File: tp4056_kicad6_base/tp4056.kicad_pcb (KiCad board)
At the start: 2 copper layers, 40 x 32 mm, 34 parts, among them J1 Conn_01x01_Female, J2 Conn_01x01_Female, J3 USB_B_Micro, J4 Conn_01x02_Male, J6 Conn_01x05_Male, Q1 AO3401A, Q2 FS8205A, Q3 AO3401A, U1 TP4056, U2 DW01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

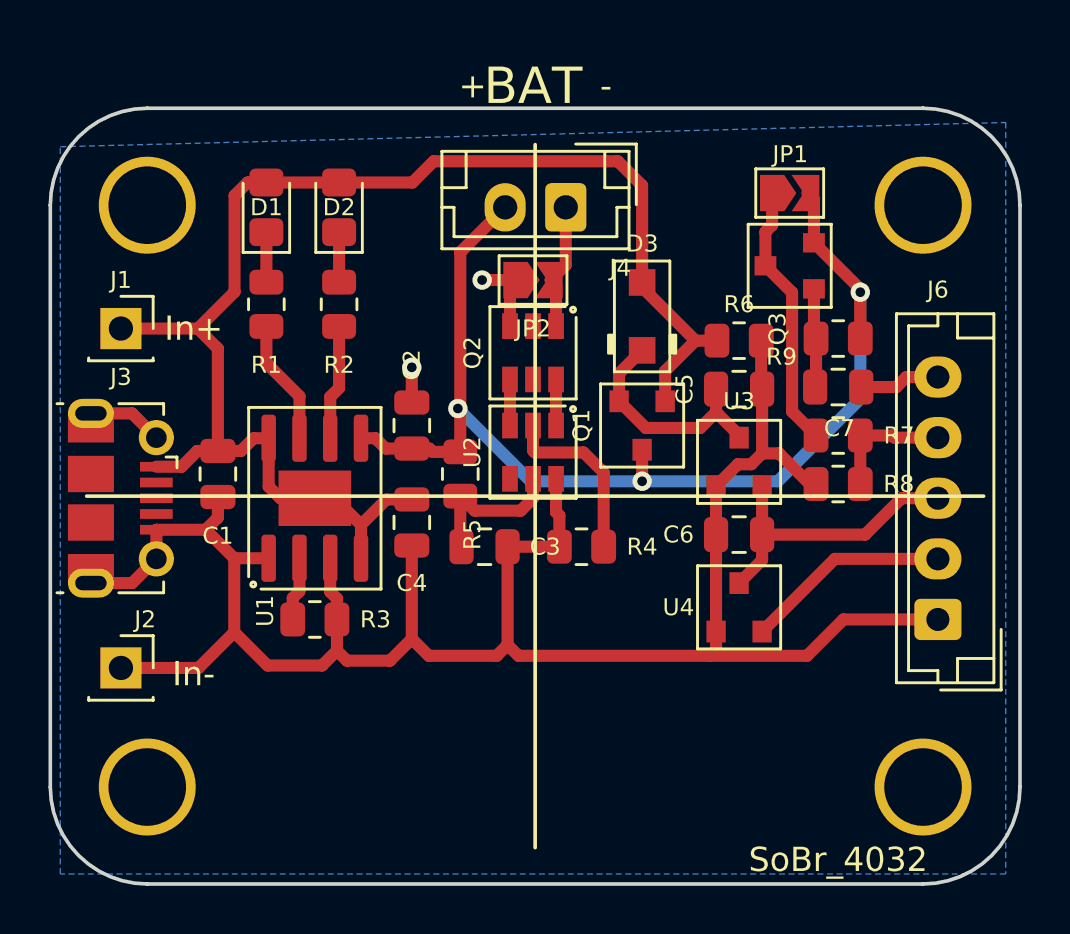
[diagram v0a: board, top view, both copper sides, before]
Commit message: PCB 40x25. To check DRC
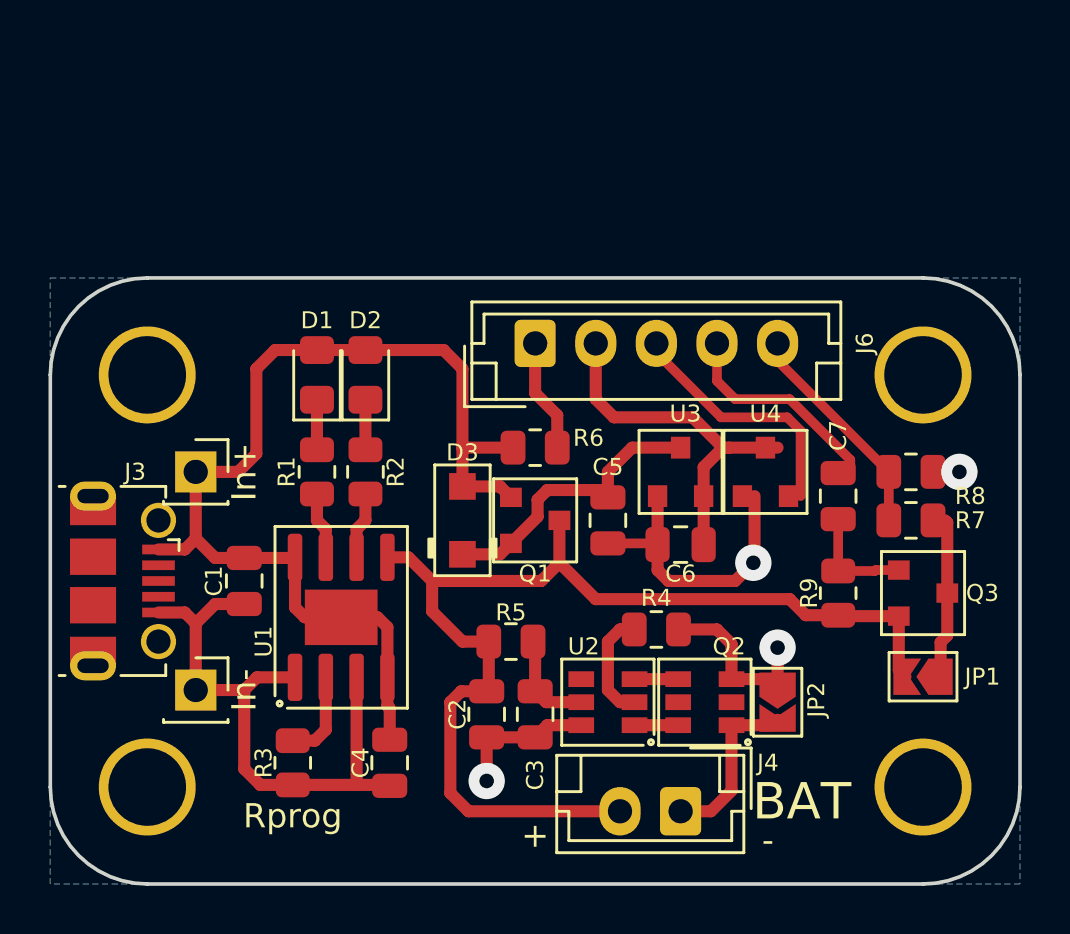
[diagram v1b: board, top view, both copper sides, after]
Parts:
- removed the REF** at (174.0, 113.0)
- added REF**: SoBr_4025, SoBr:SoBr_4025, F.Cu at (194.0, 100.5)
- moved J4 25.4 mm to (200.0, 110.0)
- moved JP1 20.7 mm to (210.0, 104.5), turned to 180 degrees
- moved J6 20.1 mm to (194.0, 90.7), turned to 0 degrees
- moved JP2 20.1 mm to (204.0, 105.5), turned to -90 degrees
- moved Q2 16.1 mm to (201.0, 105.5), turned to 180 degrees
- moved Q3 14.6 mm to (210.0, 101.0), turned to 0 degrees
- moved C2 12.3 mm to (192.0, 106.0), turned to -90 degrees
- moved D3 11.2 mm to (191.0, 98.0)
- moved U2 10.8 mm to (197.0, 105.5), turned to 180 degrees
- moved R9 10.5 mm to (206.5, 101.0), turned to 90 degrees
- moved C4 9.95 mm to (188.0, 108.0)
- moved R6 9.50 mm to (194.0, 95.0)
- moved C5 7.65 mm to (197.0, 98.0), turned to -90 degrees
- moved C3 7.22 mm to (194.0, 106.0), turned to -90 degrees
- moved D1 7.22 mm to (185.0, 92.0)
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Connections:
- J6 pad 2: /RST -> +3.3V
- J6 pad 3: +3.3V -> /RST
- J6 pad 4: /measurment -> /ena_meas
- J6 pad 5: /ena_meas -> /measurment
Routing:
- net Earth: track 92.4 -> 56.6 mm, vias 2 -> 4
- net VBUS: track 59.2 -> 44.4 mm
- net /ena_meas: track 3.33 -> 8.95 mm
- net Net-(JP1-Pad1): track 11.0 -> 6.60 mm
- net /measurment: track 5.24 -> 9.20 mm
- net Net-(R4-Pad2): track 7.38 -> 4.60 mm
- net +3.3V: track 12.3 -> 15.0 mm
- net VDC: track 9.61 -> 12.1 mm
- net Net-(R1-Pad2): track 5.18 -> 2.76 mm
- net Net-(C3-Pad1): track 6.37 -> 4.17 mm
- net Net-(R2-Pad2): track 4.76 -> 2.76 mm
- net -BATT: track 5.25 -> 7.15 mm
- net /RST: track 8.49 -> 10.4 mm
- net Net-(R3-Pad1): track 2.64 -> 3.71 mm
- net +BATT: track 47.0 -> 46.1 mm, vias 3 -> 0
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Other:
- board size 40 x 32 mm -> 40 x 25 mm
- board text added: "Rprog"

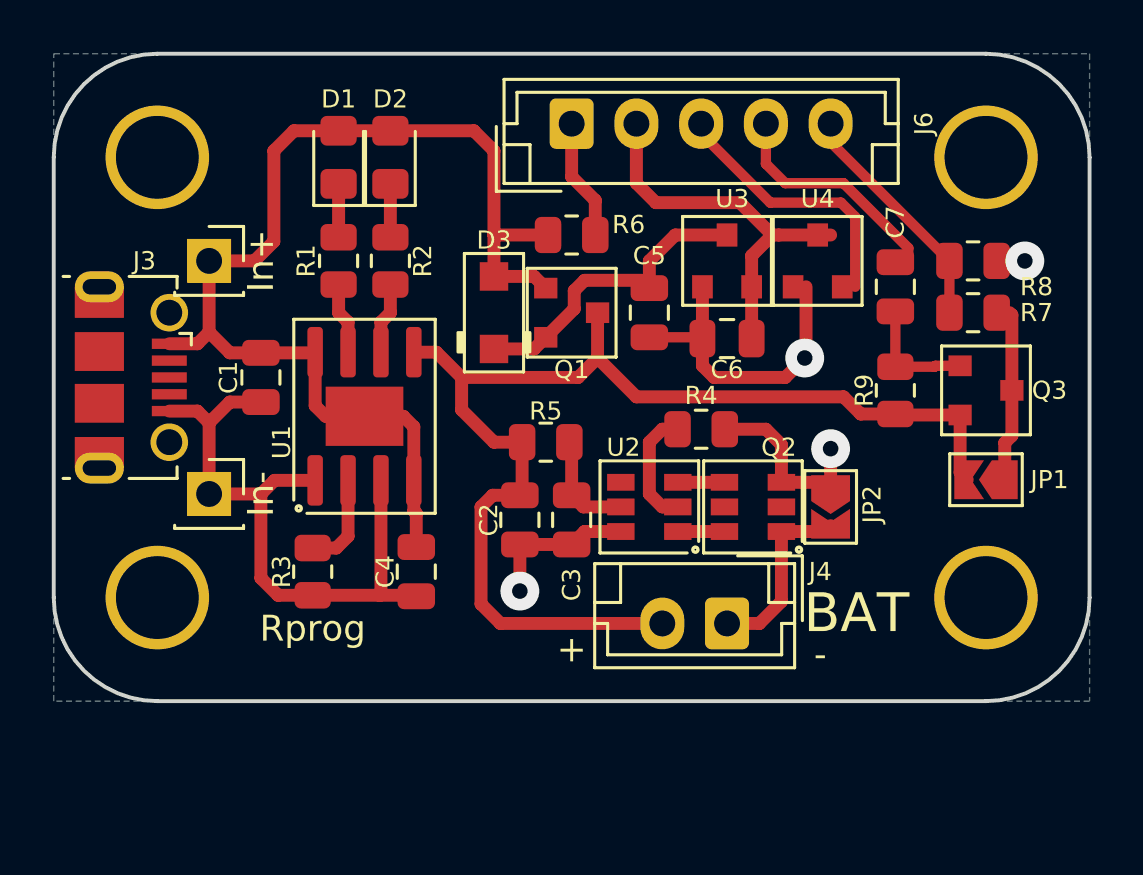
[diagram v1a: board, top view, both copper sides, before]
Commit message: SCH. Add USB and Wall Power Adaptor
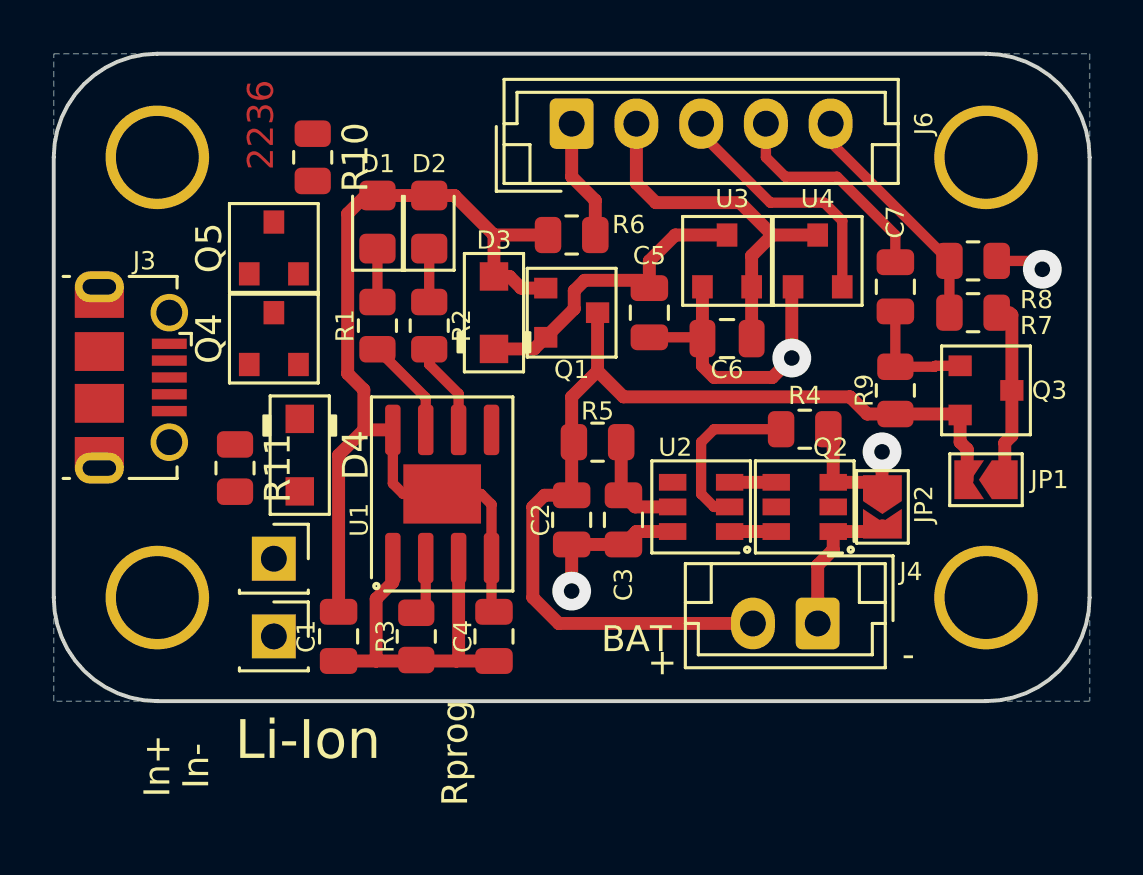
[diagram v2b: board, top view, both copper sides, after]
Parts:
- added D4: MBR1020VL, Diode_SMD_AKL:D_SOD-123F, F.Cu at (183.5, 103.5)
- added Q4: AO3401A, Package_TO_SOT_SMD_AKL:SOT-23, F.Cu at (182.5, 99.0)
- added Q5: AO3400A, Package_TO_SOT_SMD_AKL:SOT-23, F.Cu at (182.5, 95.5)
- added R10: 10k, Resistor_SMD:R_0805_2012Metric, F.Cu at (184.0, 92.0)
- added R11: 1k, Resistor_SMD:R_0805_2012Metric, F.Cu at (181.0, 104.0)
- R3: value 10k -> 2k
- moved J1 11.8 mm to (182.5, 107.5)
- moved C1 10.4 mm to (185.0, 110.5)
- moved J2 6.04 mm to (182.5, 110.5)
- moved R3 4.72 mm to (188.0, 110.5)
- moved U1 4.24 mm to (189.0, 105.0)
- moved R4 4.00 mm to (203.0, 102.5)
- moved C4 3.91 mm to (191.0, 110.5)
- moved J4 3.50 mm to (203.5, 110.0)
- moved D1 2.92 mm to (186.5, 94.5)
- moved D2 2.92 mm to (188.5, 94.5)
- moved R1 2.92 mm to (186.5, 98.5)
- moved R2 2.92 mm to (188.5, 98.5)
- moved C2 2.00 mm to (194.0, 106.0)
- moved C3 2.00 mm to (196.0, 106.0)
- moved JP2 2.00 mm to (206.0, 105.5)
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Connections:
- net Net-(R3-Pad1) renamed /Rprog
- C1 pad 1: VBUS -> VCC
- C4 pad 1: VBUS -> VCC
- D1 pad 2: VBUS -> VCC
- D2 pad 2: VBUS -> VCC
- D3 pad 2: VBUS -> VCC
- J1 pad 1: VBUS -> /Vwall
- J3 pad 1: VBUS -> /Vusb
- Q1 pad 1: VBUS -> VCC
- R6 pad 1: VBUS -> VCC
- U1 pad 4: VBUS -> VCC
- U1 pad 8: VBUS -> VCC
- U1 pad 9: VBUS -> VCC
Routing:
- net VBUS: track 44.4 -> 0.00 mm
- net VCC: track 0.00 -> 40.0 mm
- net Earth: track 56.6 -> 44.2 mm
- net +BATT: track 46.1 -> 39.0 mm
- net Net-(R4-Pad2): track 4.60 -> 6.60 mm
- net /Rprog: track 3.71 -> 2.26 mm
- net -BATT: track 7.15 -> 5.79 mm
- net Net-(R1-Pad2): track 2.76 -> 3.89 mm
- net Net-(R2-Pad2): track 2.76 -> 3.58 mm
- net /RST: track 10.4 -> 9.78 mm
- net +3.3V: track 15.0 -> 14.5 mm
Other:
- board text added: "2236"
- board text added: "Li-Ion"

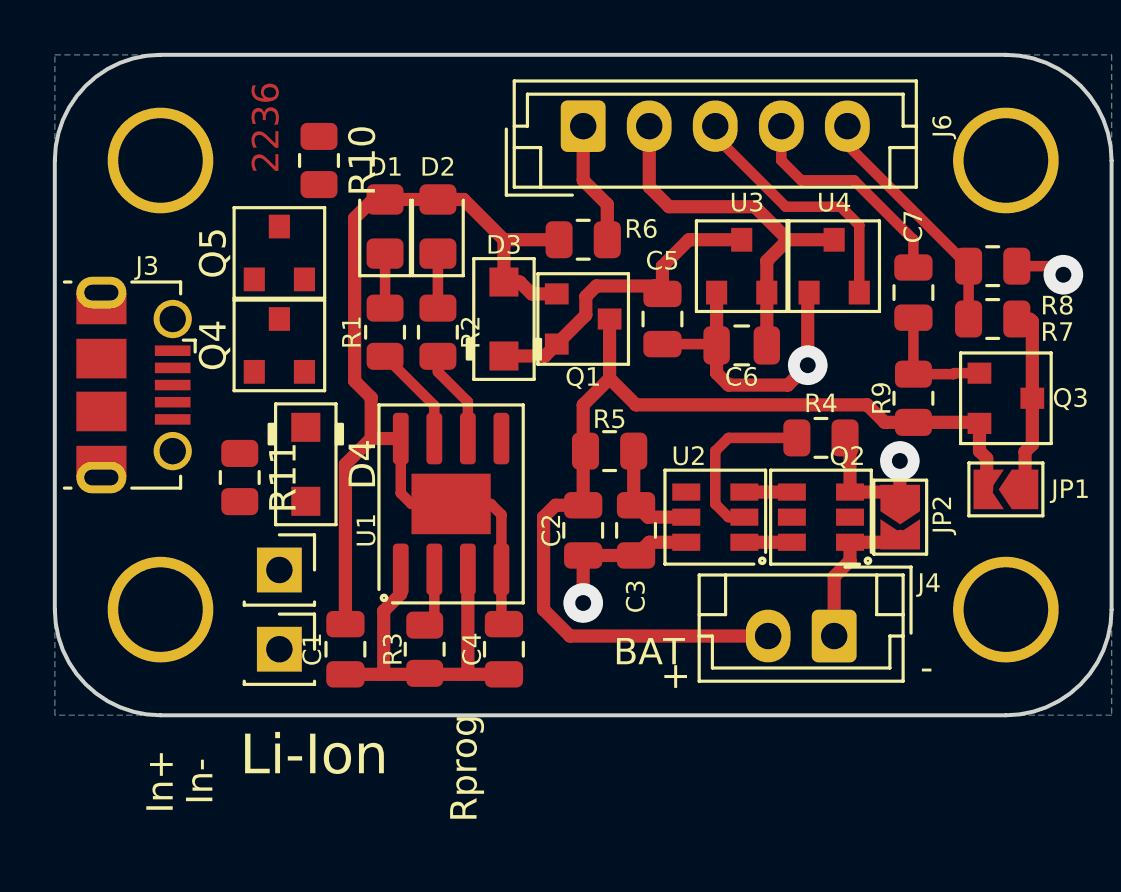
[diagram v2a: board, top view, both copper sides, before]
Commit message: PCB. 40x25. Add wall adpapter option. To final check.
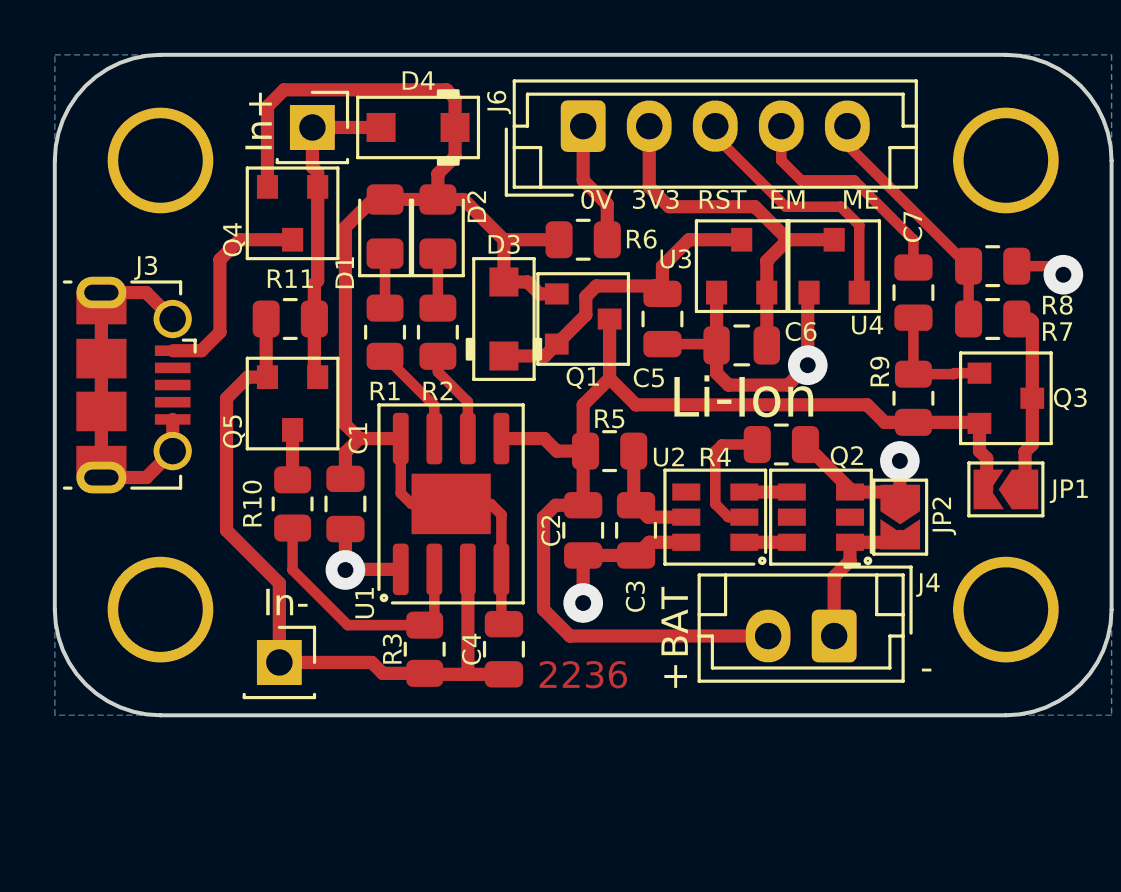
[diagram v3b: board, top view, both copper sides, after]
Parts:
- moved J1 16.8 mm to (183.8, 90.8)
- moved D4 13.4 mm to (187.8, 90.8), turned to 180 degrees
- moved R10 13.0 mm to (183.0, 105.0), turned to 90 degrees
- moved R11 6.30 mm to (182.9, 98.0), turned to 0 degrees
- moved Q5 5.72 mm to (183.0, 101.2), turned to -90 degrees
- moved C1 5.50 mm to (185.0, 105.0)
- moved Q4 5.02 mm to (183.0, 94.0), turned to -90 degrees
- moved R4 1.52 mm to (201.5, 102.8)
- moved J2 0.50 mm to (182.5, 111.0)
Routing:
- net Earth: track 44.2 -> 76.0 mm, vias 4 -> 5
- net /Vwall: track 0.00 -> 12.2 mm
- net VCC: track 40.0 -> 49.5 mm
- net /Vusb: track 0.00 -> 7.89 mm
- net /Rprog: track 2.26 -> 9.72 mm
- net +BATT: track 39.0 -> 42.3 mm
- net Net-(Q5-Pad3): track 0.00 -> 1.89 mm
- net Net-(R4-Pad2): track 6.60 -> 5.00 mm
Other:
- board text added: "0V"
- board text added: "3V3"
- board text added: "EM"
- board text added: "ME"
- board text added: "RST"
- board text removed: "Rprog"

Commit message: PCB. output files. minor cosmetic changes.
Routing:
- net Earth: track 76.0 -> 77.1 mm
- net /measurment: track 9.20 -> 8.49 mm
- net VCC: track 49.5 -> 48.9 mm
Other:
- board text added: "B.Cu"
- board text added: "B.Silkscreen"
- board text added: "B.SolderMask"
- board text added: "Board"
- board text added: "Drawings"
- board text added: "F.Cu"
- board text added: "F.Silkscreen"
- board text added: "F.SolderMask"
